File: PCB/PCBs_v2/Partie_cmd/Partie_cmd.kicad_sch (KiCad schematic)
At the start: 54 parts, among them J1 Barrel_Jack, J2 Conn_01x04_Socket, J3 Conn_01x04_Socket, J4 Conn_01x11_Pin, J5 Conn_01x10_Pin, SW1 SW_MEC_5G, U1 ESP32-S3-DEVKITC-1-N8R2, U3 BU33SD5WG-TR, U4 XL1509-5.0

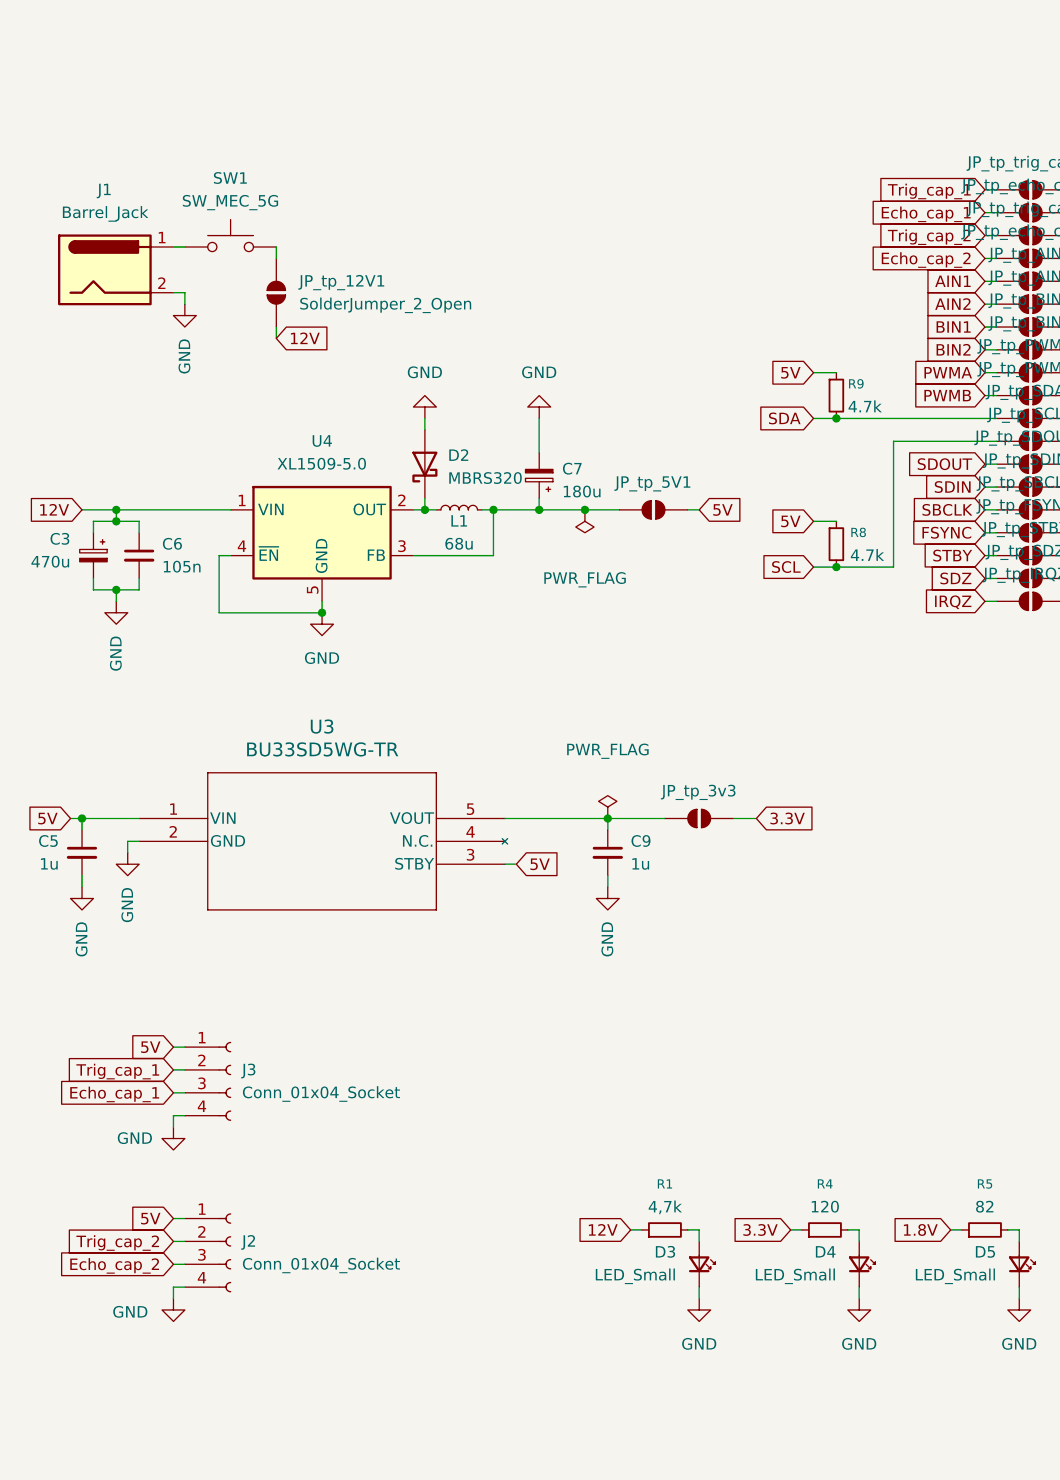
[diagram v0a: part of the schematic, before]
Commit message: Add new KiCad PCB and schematic files for Partie_cmd
Added new footprints, backup files, and autosave files for the Partie_cmd project in PCBs_v2, including ESP32 and SSOP5 footprints. Updated Partie_cmd.kicad_pcb, Partie_cmd.kicad_sch, and fp-lib-table to reflect new components and changes. Also added autosave and lock files for both PCB_v1 and PCBs_v2 projects.
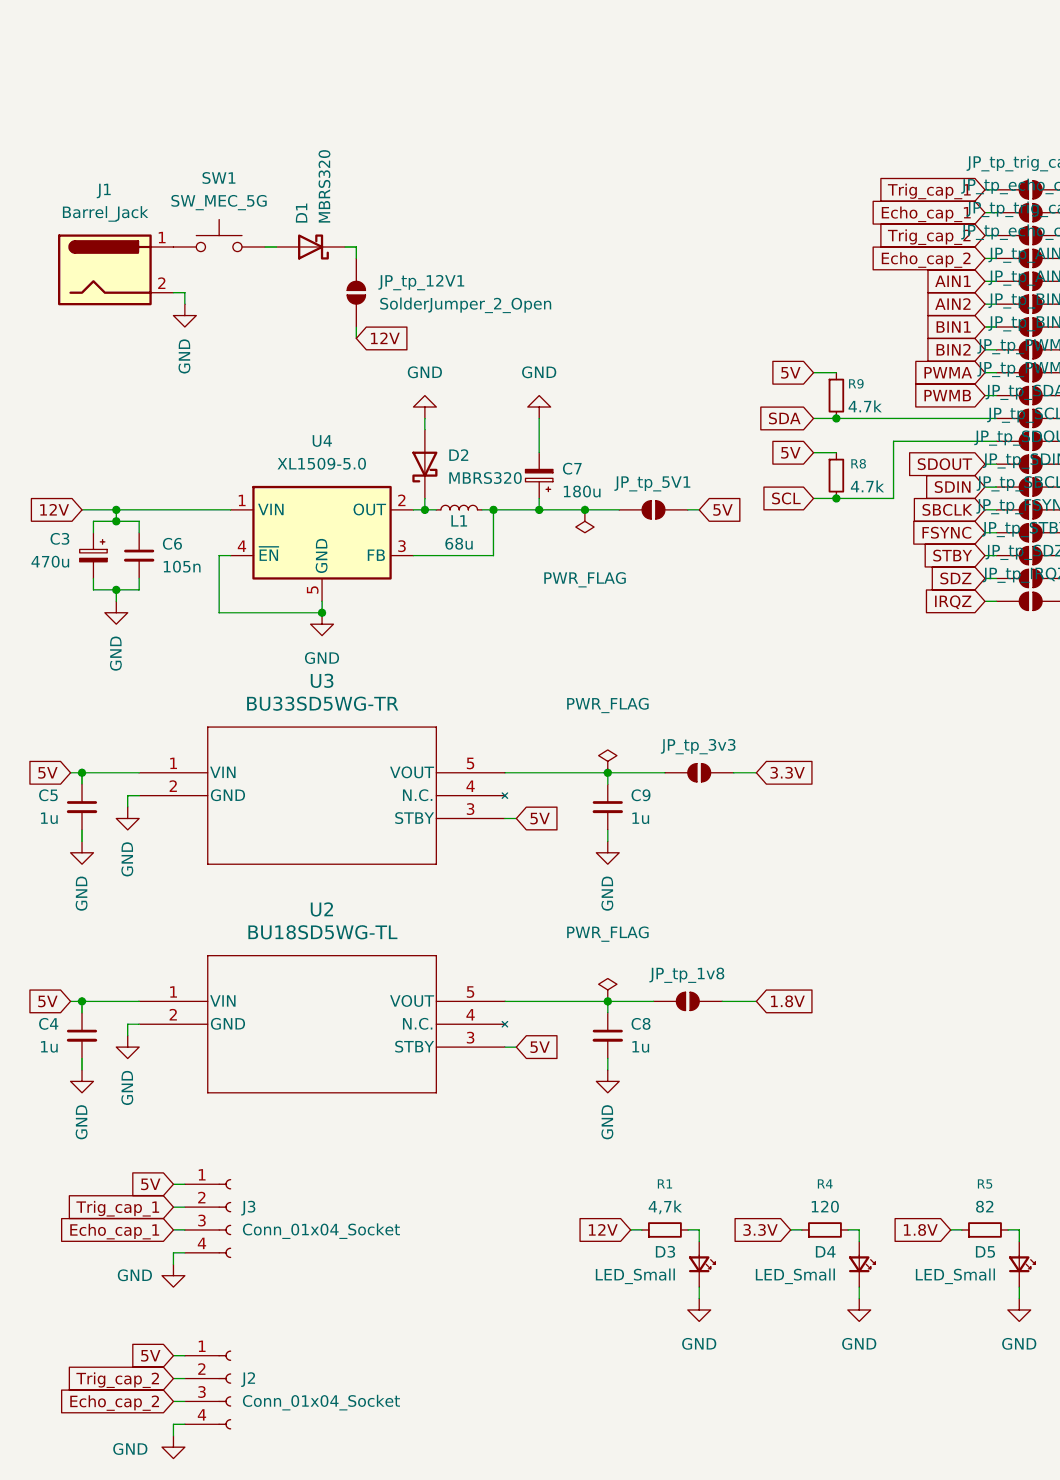
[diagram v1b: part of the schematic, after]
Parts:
- added C4, C8: 1u, Capacitor_SMD:C_0603_1608Metric_Pad1.08x0.95mm_HandSolder, symbol Device:C_Small
- added D1: MBRS320, Diode_SMD:D_SMC, symbol Diode:1N5820
- added JP_tp_1v8: SolderJumper_2_Open, Jumper:SolderJumper-2_P1.3mm_Open_TrianglePad1.0x1.5mm, symbol Jumper:SolderJumper_2_Open
- added U2: BU18SD5WG-TL, footprints:SSOP5_ROM-L, symbol 2025-09-19_12-33-54:BU18SD5WG-TL
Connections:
- net 1.8V: now also JP_tp_1v8.2 (B)
- net 5V: now also C4.1, U2.1 (VIN), U2.3 (STBY)
- net GND: now also C4.2, C8.2, U2.2 (GND)
- net at SW1.3 (B), SW1.4 (B): now also D1.2 (A); no longer JP_tp_12V1.1 (A)
- new net: C8.1, JP_tp_1v8.1 (A), U2.5 (VOUT)
- new net: D1.1 (K), JP_tp_12V1.1 (A)
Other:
- moved on the sheet: C5, C9, J2, J3, JP_tp_12V1, JP_tp_3v3, R8, SW1, U3

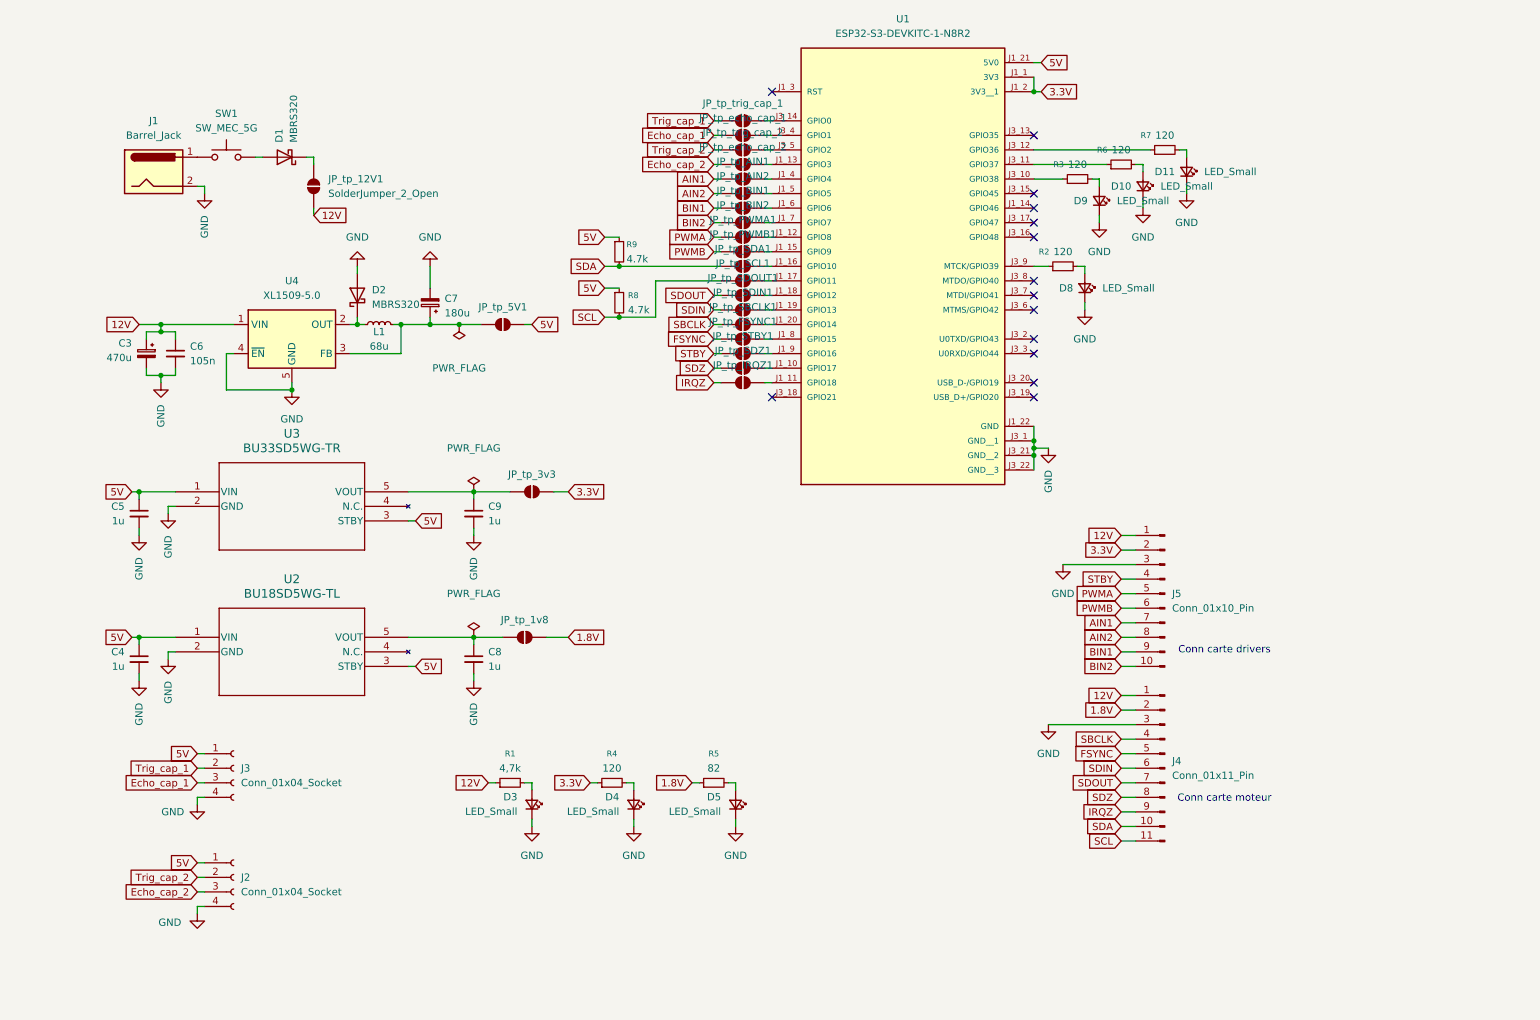
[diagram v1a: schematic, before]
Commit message: fin schéma + Routage PCB cmd
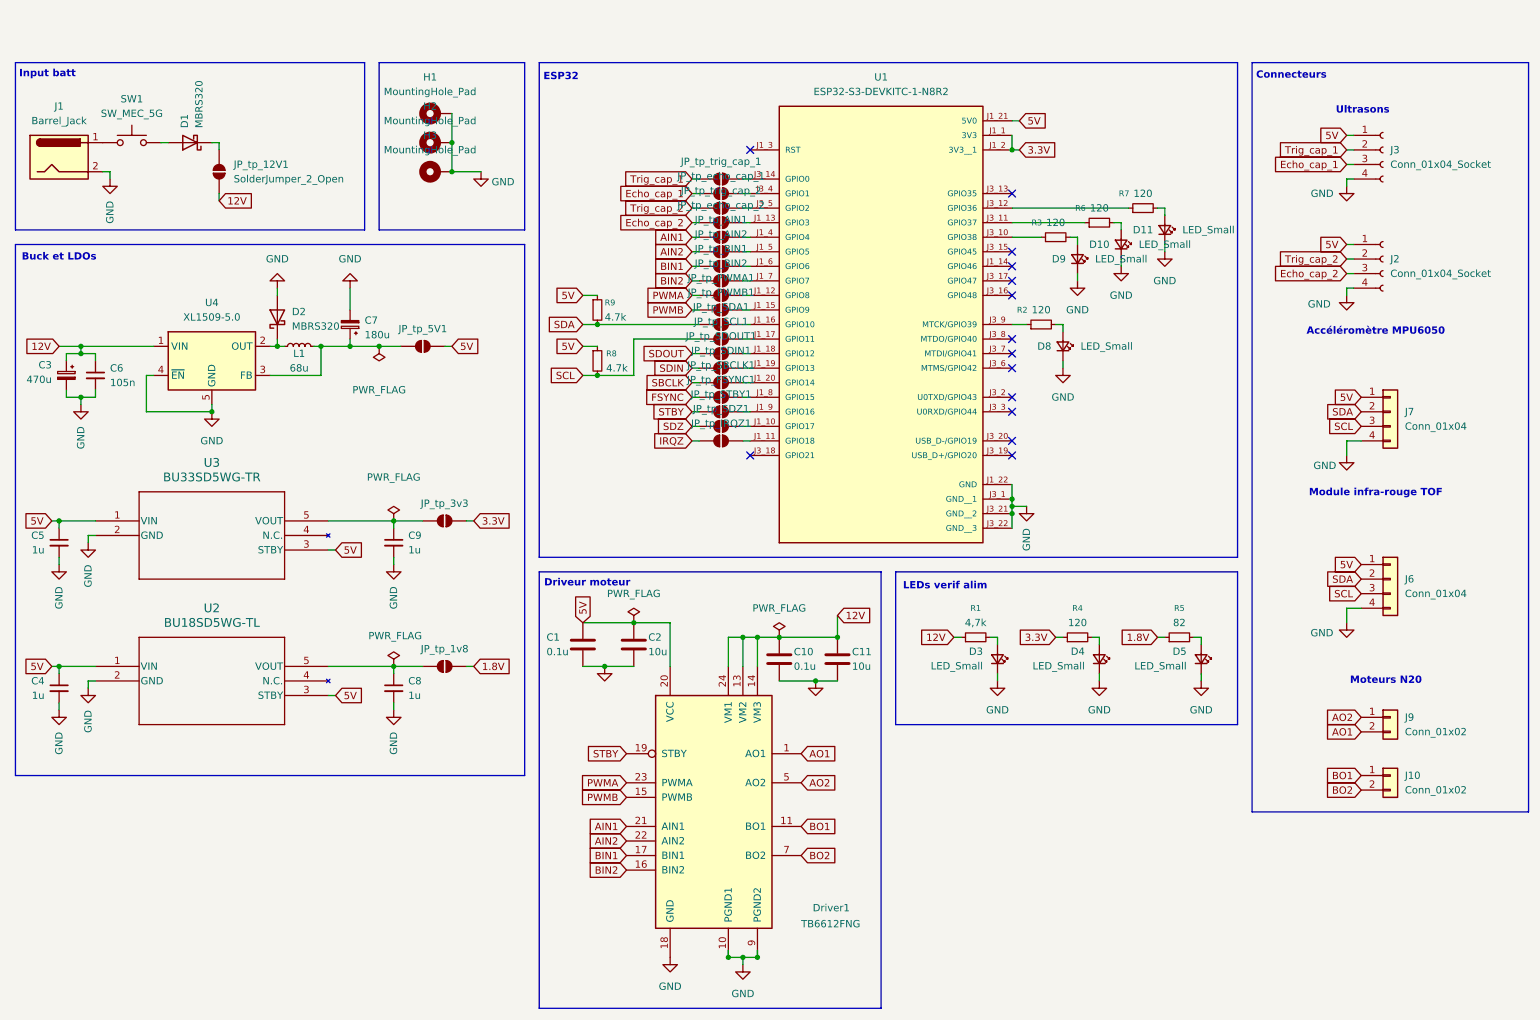
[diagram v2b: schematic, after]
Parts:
- removed J4: Conn_01x11_Pin, Connector_PinHeader_1.00mm:PinHeader_1x10_P1.00mm_Vertical, symbol Connector:Conn_01x11_Pin
- removed J5: Conn_01x10_Pin, Connector_PinHeader_1.00mm:PinHeader_1x11_P1.00mm_Vertical, symbol Connector:Conn_01x10_Pin
- added C1, C10: 0.1u, Capacitor_SMD:C_0402_1005Metric, symbol Device:C
- added C11, C2: 10u, Capacitor_SMD:C_0805_2012Metric, symbol Device:C
- added Driver1: TB6612FNG, Package_SO:SSOP-24_5.3x8.2mm_P0.65mm, symbol Driver_Motor:TB6612FNG
- added H1, H2, H3: MountingHole_Pad, MountingHole:MountingHole_2.5mm_Pad_Via, symbol Mechanical:MountingHole_Pad
- added J10, J9: Conn_01x02, Connector_JST:JST_XH_B2B-XH-A_1x02_P2.50mm_Vertical, symbol Connector_Generic:Conn_01x02
- added J6, J7: Conn_01x04, Connector_PinSocket_1.00mm:PinSocket_1x04_P1.00mm_Vertical, symbol Connector_Generic:Conn_01x04
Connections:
- net 12V: now also C10.1, C11.1, Driver1.13 (VM2), Driver1.14 (VM3), Driver1.24 (VM1)
- net 5V: now also C1.1, C2.1, Driver1.20 (VCC), J6.1 (Pin_1), J7.1 (Pin_1)
- net AIN1: now also Driver1.21 (AIN1)
- net AIN2: now also Driver1.22 (AIN2)
- net BIN1: now also Driver1.17 (BIN1)
- net BIN2: now also Driver1.16 (BIN2)
- net GND: now also C1.2, C10.2, C11.2, C2.2, Driver1.10 (PGND2), Driver1.18 (GND), Driver1.4 (PGND1), Driver1.9 (PGND2), H1.1, H2.1, H3.1, J6.4 (Pin_4), J7.4 (Pin_4)
- net PWMA: now also Driver1.23 (PWMA)
- net PWMB: now also Driver1.15 (PWMB)
- net SCL: now also J6.3 (Pin_3), J7.3 (Pin_3)
- net SDA: now also J6.2 (Pin_2), J7.2 (Pin_2)
- net STBY: now also Driver1.19 (STBY)
- new net AO1: Driver1.1 (AO1), Driver1.2 (AO1), J9.2 (Pin_2)
- new net AO2: Driver1.5 (AO2), Driver1.6 (AO2), J9.1 (Pin_1)
- new net BO1: Driver1.11 (BO1), Driver1.12 (BO1), J10.1 (Pin_1)
- new net BO2: Driver1.7 (BO2), Driver1.8 (BO2), J10.2 (Pin_2)
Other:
- note added: "Accéléromètre MPU6050"
- note added: "Buck et LDOs"
- note added: "Connecteurs"
- note added: "Driveur moteur"
- note added: "ESP32"
- note added: "Input batt"
- note added: "LEDs verif alim"
- note added: "Module infra-rouge TOF"
- note added: "Moteurs N20"
- note added: "Ultrasons"
- note removed: "Conn carte drivers"
- note removed: "Conn carte moteur"
- moved on the sheet: C3, C4, C5, C6, C7, C8, C9, D1, D10, D11, D2, D3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

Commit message: Routage pcb cmd
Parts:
- removed SW1: SW_MEC_5G, symbol Switch:SW_MEC_5G
- added D6: LED_Small, LED_SMD:LED_0603_1608Metric_Pad1.05x0.95mm_HandSolder, symbol Device:LED_Small
- added H4, H5: MountingHole_Pad, MountingHole:MountingHole_2.2mm_M2_DIN965_Pad, symbol Mechanical:MountingHole_Pad
- added J4: Conn_01x13_Pin, Connector_PinHeader_1.27mm:PinHeader_1x13_P1.27mm_Vertical, symbol Connector:Conn_01x13_Pin
- added JP1: Jumper_2_Bridged, TestPoint:TestPoint_2Pads_Pitch2.54mm_Drill0.8mm, symbol Jumper:Jumper_2_Bridged
- added R10: 1.2k, Resistor_SMD:R_0603_1608Metric_Pad0.98x0.95mm_HandSolder, symbol Device:R_Small
- J1: footprint (none) -> Connector_BarrelJack:BarrelJack_Wuerth_694108106102_2.5x5.5mm
- R4: value 120 -> 1.2k
- R5: value 82 -> 820
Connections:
- net 1.8V: now also J4.9 (Pin_9)
- net 12V: now also J4.11 (Pin_11)
- net 3.3V: now also C1.1, C2.1, Driver1.20 (VCC), R10.1; no longer R4.1
- net 5V: now also R4.1, J4.10 (Pin_10); no longer C1.1, C2.1, Driver1.20 (VCC)
- net FSYNC: now also J4.1 (Pin_1)
- net GND: now also Driver1.3 (PGND1), D6.1 (K), H4.1, H5.1, J4.12 (Pin_12), J4.13 (Pin_13)
- net IRQZ: now also J4.7 (Pin_7)
- net SBCLK: now also J4.2 (Pin_2)
- net SCL: now also J4.4 (Pin_4)
- net SDA: now also J4.5 (Pin_5)
- net SDIN: now also J4.3 (Pin_3)
- net SDOUT: now also J4.8 (Pin_8)
- net SDZ: now also J4.6 (Pin_6)
- net at J1.1: now also JP1.1 (A)
- net at D1.2 (A): now also JP1.2 (B)
- new net: D6.2 (A), R10.2
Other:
- note added: "Conn carte audio"

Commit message: Fin routage pcb cmd
:(
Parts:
- removed J4: Conn_01x13_Pin, Connector_PinHeader_1.27mm:PinHeader_1x13_P1.27mm_Vertical, symbol Connector:Conn_01x13_Pin
- removed J7: Conn_01x04, Connector_PinSocket_1.00mm:PinSocket_1x04_P1.00mm_Vertical, symbol Connector_Generic:Conn_01x04
- added J4: Conn_01x12, Connector_PinHeader_1.27mm:PinHeader_1x12_P1.27mm_Vertical, symbol Connector_Generic:Conn_01x12
- added J5: Conn_01x04, symbol Connector_Generic:Conn_01x04
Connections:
- net 1.8V: now also J4.3 (Pin_3)
- net 12V: now also J4.12 (Pin_12)
- net 5V: now also J4.10 (Pin_10)
- net FSYNC: now also J4.7 (Pin_7)
- net GND: now also J4.11 (Pin_11)
- net IRQZ: now also J4.2 (Pin_2)
- net SBCLK: now also J4.6 (Pin_6)
- net SCL: now also J4.5 (Pin_5)
- net SDA: now also J4.4 (Pin_4)
- net SDIN: now also J4.8 (Pin_8)
- net SDOUT: now also J4.9 (Pin_9)
- net SDZ: now also J4.1 (Pin_1)
- no-connect marks 14 -> 18

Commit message: Fin routage 1.2
pour de vrai cette foix?
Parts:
- removed J5: Conn_01x04, symbol Connector_Generic:Conn_01x04
- added J7: Conn_01x04, Connector_PinHeader_1.27mm:PinHeader_1x04_P1.27mm_Vertical, symbol Connector_Generic:Conn_01x04
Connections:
- net 5V: now also J7.1 (Pin_1)
- net GND: now also J7.2 (Pin_2)
- net SCL: now also J7.4 (Pin_4)
- net SDA: now also J7.3 (Pin_3)
- no-connect marks 18 -> 14
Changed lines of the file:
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@@
 	)
 	(no_connect
-		(at 254 91.44)
-	)
-	(no_connect
 		(at 193.04 91.44)
 	)
@@
 	)
 	(no_connect
-		(at 254 99.06)
-	)
-	(no_connect
-		(at 254 96.52)
-	)
-	(no_connect
-		(at 254 93.98)
-	)
-	(no_connect
 		(at 193.04 81.28)
 	)
@@
 	)
 	(symbol
-		(lib_id "Connector_Generic:Conn_01x04")
-		(at 2346.96 194.31 0)
-		(unit 1)
-		(exclude_from_sim no)
-		(in_bom yes)
-		(on_board yes)
-		(dnp no)
-		(fields_autoplaced yes)
-		(property "Reference" "J5"
-			(at 2349.5 194.3099 0)
-			(effects
-				(font
-					(size 1.27 1.27)
-				)
-				(justify left)
-			)
-		)
-		(property "Value" "Conn_01x04"
-			(at 2349.5 196.8499 0)
-			(effects
-				(font
-					(size 1.27 1.27)
-				)
-				(justify left)
-			)
-		)
-		(property "Footprint" ""
-			(at 2346.96 194.31 0)
-			(effects
-				(font
-					(size 1.27 1.27)
-				)
-				(hide yes)
-			)
-		)
-		(property "Datasheet" "~"
-			(at 2346.96 194.31 0)
-			(effects
-				(font
-					(size 1.27 1.27)
-				)
-				(hide yes)
-			)
-		)
-		(property "Description" "Generic connector, single row, 01x04, script generated (kicad-library-utils/schlib/autogen/connector/)"
-			(at 2346.96 194.31 0)
-			(effects
-				(font
-					(size 1.27 1.27)
-				)
-				(hide yes)
-			)
-		)
-		(pin "2"
-		)
-		(pin "4"
-		)
-		(pin "1"
-		)
-		(pin "3"
-		)
-		(instances
-			(project ""
-				(path "/feb16e15-81d7-49b9-8315-2aeb60da597a"
-					(reference "J5")
-					(unit 1)
-				)
-			)
-		)
-	)
-	(symbol
 		(lib_id "Device:LED_Small")
 		(at 190.5 127 270)
@@
 					(unit 1)
 				)
+			)
+		)
+	)
+	(symbol
+		(lib_id "Connector_Generic:Conn_01x04")
+		(at 259.08 83.82 0)
+		(unit 1)
+		(exclude_from_sim no)
+		(in_bom yes)
+		(on_board yes)
+		(dnp no)
+		(fields_autoplaced yes)
+		(property "Reference" "J7"
+			(at 261.62 83.8199 0)
+			(effects
+				(font
+					(size 1.27 1.27)
+				)
+				(justify left)
+			)
+		)
+		(property "Value" "Conn_01x04"
+			(at 261.62 86.3599 0)
+			(effects
+				(font
+					(size 1.27 1.27)
+				)
+				(justify left)
+			)
+		)
+		(property "Footprint" "Connector_PinHeader_1.27mm:PinHeader_1x04_P1.27mm_Vertical"
+			(at 259.08 83.82 0)
+			(effects
+				(font
+					(size 1.27 1.27)
+				)
+				(hide yes)
+			)
+		)
+		(property "Datasheet" "~"
+			(at 259.08 83.82 0)
+			(effects
+				(font
+					(size 1.27 1.27)
+				)
+				(hide yes)
+			)
+		)
+		(property "Description" "Generic connector, single row, 01x04, script generated (kicad-library-utils/schlib/autogen/connector/)"
+			(at 259.08 83.82 0)
+			(effects
+				(font
+					(size 1.27 1.27)
+				)
+				(hide yes)
+			)
+		)
+		(pin "1"
+		)
+		(pin "3"
+		)
+		(pin "4"
+		)
+		(pin "2"
+		)
+		(instances
+			(project ""
+				(path "/feb16e15-81d7-49b9-8315-2aeb60da597a"
+					(reference "J7")
+					(unit 1)
+				)
